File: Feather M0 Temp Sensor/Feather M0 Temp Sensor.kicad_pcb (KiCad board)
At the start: 2 copper layers, 40.6 x 25.4 mm, 3 parts, among them J1 Feather_Long_Side, J2 Feather_Short_Side, U1 Adafruit_SHT4x

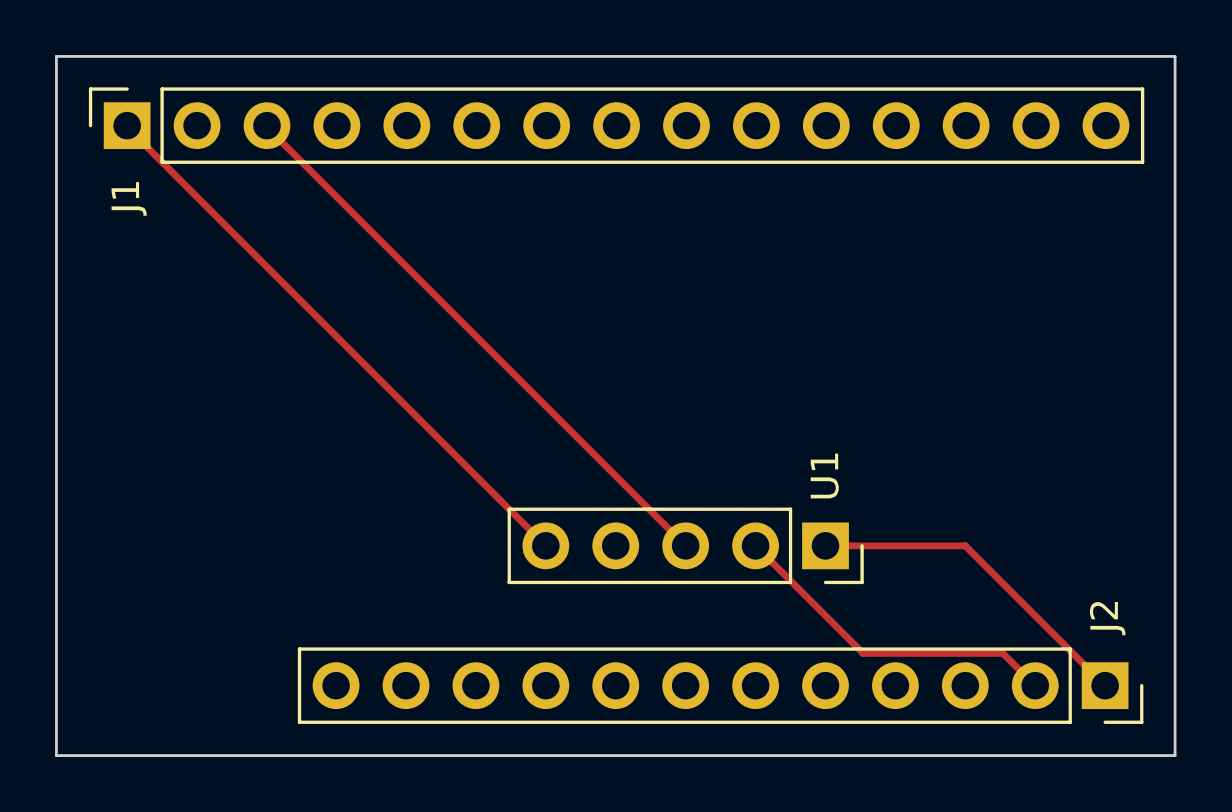
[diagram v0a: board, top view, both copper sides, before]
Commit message: Improved PCB look
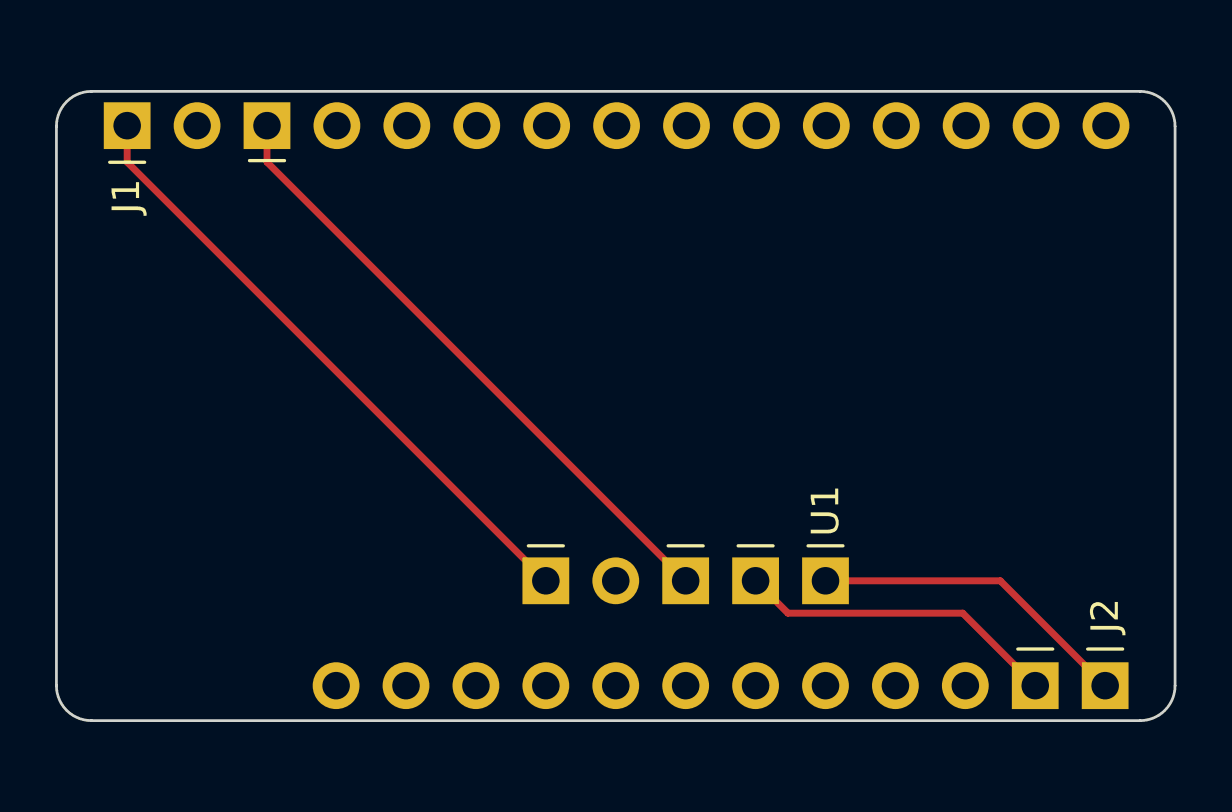
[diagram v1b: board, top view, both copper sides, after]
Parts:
- moved U1 1.27 mm to (119.4, 72.4)
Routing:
- net Net-(U1-Pad5): track 21.6 -> 22.8 mm
- net Net-(U1-Pad3): track 21.6 -> 22.8 mm
- net Net-(U1-Pad2): track 12.3 -> 11.7 mm
- net Net-(U1-Pad1): track 12.3 -> 11.7 mm
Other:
- board size 40.6 x 25.4 mm -> 40.6 x 22.9 mm
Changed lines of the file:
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@@
       (effects (font (size 1 1) (thickness 0.15)))
     )
-    (fp_line (start -1.33 1.27) (end -1.33 36.89) (layer "F.SilkS") (width 0.12))
-    (fp_line (start -1.33 36.89) (end 1.33 36.89) (layer "F.SilkS") (width 0.12))
-    (fp_line (start 0 -1.33) (end 1.33 -1.33) (layer "F.SilkS") (width 0.12))
-    (fp_line (start -1.33 1.27) (end 1.33 1.27) (layer "F.SilkS") (width 0.12))
-    (fp_line (start 1.33 1.27) (end 1.33 36.89) (layer "F.SilkS") (width 0.12))
-    (fp_line (start 1.33 -1.33) (end 1.33 0) (layer "F.SilkS") (width 0.12))
+    (fp_line (start -1.33 -0.635) (end -1.33 0.635) (layer "F.SilkS") (width 0.12))
+    (fp_line (start -1.27 4.445) (end -1.27 5.715) (layer "F.SilkS") (width 0.12))
     (fp_line (start 1.75 -1.8) (end 1.75 37.3) (layer "F.CrtYd") (width 0.05))
     (fp_line (start -1.8 -1.8) (end 1.75 -1.8) (layer "F.CrtYd") (width 0.05))
     (fp_line (start 1.75 37.3) (end -1.8 37.3) (layer "F.CrtYd") (width 0.05))
     (fp_line (start -1.8 37.3) (end -1.8 -1.8) (layer "F.CrtYd") (width 0.05))
-    (fp_line (start 1.27 -0.635) (end 1.27 36.83) (layer "F.Fab") (width 0.1))
-    (fp_line (start 0.635 -1.27) (end 1.27 -0.635) (layer "F.Fab") (width 0.1))
-    (fp_line (start -1.27 36.83) (end -1.27 -1.27) (layer "F.Fab") (width 0.1))
-    (fp_line (start 1.27 36.83) (end -1.27 36.83) (layer "F.Fab") (width 0.1))
-    (fp_line (start -1.27 -1.27) (end 0.635 -1.27) (layer "F.Fab") (width 0.1))
     (pad "1" thru_hole rect (at 0 0 90) (size 1.7 1.7) (drill 1) (layers *.Cu *.Mask)
       (net 5 "Net-(U1-Pad5)") (pinfunction "3V") (pintype "power_out"))
     (pad "2" thru_hole oval (at 0 2.54 90) (size 1.7 1.7) (drill 1) (layers *.Cu *.Mask)
       (net 6 "unconnected-(J1-Pad2)") (pinfunction "Pin_2") (pintype "passive"))
-    (pad "3" thru_hole oval (at 0 5.08 90) (size 1.7 1.7) (drill 1) (layers *.Cu *.Mask)
+    (pad "3" thru_hole rect (at 0 5.08 90) (size 1.7 1.7) (drill 1) (layers *.Cu *.Mask)
       (net 3 "Net-(U1-Pad3)") (pinfunction "GND") (pintype "power_out"))
     (pad "4" thru_hole oval (at 0 7.62 90) (size 1.7 1.7) (drill 1) (layers *.Cu *.Mask)
@@
   )
   (footprint "Connector_PinSocket_2.54mm:PinSocket_1x05_P2.54mm_Vertical" (layer "F.Cu")
-    (at 119.38 71.12 -90)
+    (at 119.38 72.39 -90)
     (descr "Through hole straight socket strip, 1x05, 2.54mm pitch, single row (from Kicad 4.0.7), script generated")
     (tags "Through hole socket strip THT 1x05 2.54mm single row")
@@
       (effects (font (size 1 1) (thickness 0.15)))
     )
-    (fp_line (start 1.33 1.27) (end 1.33 11.49) (layer "F.SilkS") (width 0.12))
-    (fp_line (start -1.33 11.49) (end 1.33 11.49) (layer "F.SilkS") (width 0.12))
-    (fp_line (start -1.33 1.27) (end 1.33 1.27) (layer "F.SilkS") (width 0.12))
-    (fp_line (start -1.33 1.27) (end -1.33 11.49) (layer "F.SilkS") (width 0.12))
-    (fp_line (start 0 -1.33) (end 1.33 -1.33) (layer "F.SilkS") (width 0.12))
-    (fp_line (start 1.33 -1.33) (end 1.33 0) (layer "F.SilkS") (width 0.12))
+    (fp_line (start -1.27 9.525) (end -1.27 10.795) (layer "F.SilkS") (width 0.12))
+    (fp_line (start -1.27 1.905) (end -1.27 3.175) (layer "F.SilkS") (width 0.12))
+    (fp_line (start -1.27 4.445) (end -1.27 5.715) (layer "F.SilkS") (width 0.12))
+    (fp_line (start -1.27 -0.635) (end -1.27 0.635) (layer "F.SilkS") (width 0.12))
     (fp_line (start 1.75 -1.8) (end 1.75 11.9) (layer "F.CrtYd") (width 0.05))
     (fp_line (start -1.8 11.9) (end -1.8 -1.8) (layer "F.CrtYd") (width 0.05))
     (fp_line (start 1.75 11.9) (end -1.8 11.9) (layer "F.CrtYd") (width 0.05))
     (fp_line (start -1.8 -1.8) (end 1.75 -1.8) (layer "F.CrtYd") (width 0.05))
-    (fp_line (start -1.27 -1.27) (end 0.635 -1.27) (layer "F.Fab") (width 0.1))
-    (fp_line (start 1.27 11.43) (end -1.27 11.43) (layer "F.Fab") (width 0.1))
-    (fp_line (start -1.27 11.43) (end -1.27 -1.27) (layer "F.Fab") (width 0.1))
-    (fp_line (start 0.635 -1.27) (end 1.27 -0.635) (layer "F.Fab") (width 0.1))
-    (fp_line (start 1.27 -0.635) (end 1.27 11.43) (layer "F.Fab") (width 0.1))
     (pad "1" thru_hole rect (at 0 0 270) (size 1.7 1.7) (drill 1) (layers *.Cu *.Mask)
       (net 1 "Net-(U1-Pad1)") (pinfunction "SDA") (pintype "bidirectional"))
-    (pad "2" thru_hole oval (at 0 2.54 270) (size 1.7 1.7) (drill 1) (layers *.Cu *.Mask)
+    (pad "2" thru_hole rect (at 0 2.54 270) (size 1.7 1.7) (drill 1) (layers *.Cu *.Mask)
       (net 2 "Net-(U1-Pad2)") (pinfunction "SCL") (pintype "input"))
-    (pad "3" thru_hole oval (at 0 5.08 270) (size 1.7 1.7) (drill 1) (layers *.Cu *.Mask)
+    (pad "3" thru_hole rect (at 0 5.08 270) (size 1.7 1.7) (drill 1) (layers *.Cu *.Mask)
       (net 3 "Net-(U1-Pad3)") (pinfunction "GND") (pintype "power_in"))
     (pad "4" thru_hole oval (at 0 7.62 270) (size 1.7 1.7) (drill 1) (layers *.Cu *.Mask)
       (net 4 "unconnected-(U1-Pad4)") (pinfunction "3V") (pintype "power_out"))
-    (pad "5" thru_hole oval (at 0 10.16 270) (size 1.7 1.7) (drill 1) (layers *.Cu *.Mask)
+    (pad "5" thru_hole rect (at 0 10.16 270) (size 1.7 1.7) (drill 1) (layers *.Cu *.Mask)
       (net 5 "Net-(U1-Pad5)") (pinfunction "VIN") (pintype "power_in"))
     (model "${KICAD6_3DMODEL_DIR}/Connector_PinSocket_2.54mm.3dshapes/PinSocket_1x05_P2.54mm_Vertical.wrl"
@@
       (effects (font (size 1 1) (thickness 0.15)))
     )
-    (fp_line (start 1.33 1.27) (end 1.33 29.27) (layer "F.SilkS") (width 0.12))
-    (fp_line (start 0 -1.33) (end 1.33 -1.33) (layer "F.SilkS") (width 0.12))
-    (fp_line (start -1.33 1.27) (end -1.33 29.27) (layer "F.SilkS") (width 0.12))
-    (fp_line (start -1.33 1.27) (end 1.33 1.27) (layer "F.SilkS") (width 0.12))
-    (fp_line (start 1.33 -1.33) (end 1.33 0) (layer "F.SilkS") (width 0.12))
-    (fp_line (start -1.33 29.27) (end 1.33 29.27) (layer "F.SilkS") (width 0.12))
+    (fp_line (start -1.33 -0.635) (end -1.33 0.635) (layer "F.SilkS") (width 0.12))
+    (fp_line (start -1.33 1.905) (end -1.33 3.175) (layer "F.SilkS") (width 0.12))
     (fp_line (start -1.8 29.7) (end -1.8 -1.8) (layer "F.CrtYd") (width 0.05))
     (fp_line (start -1.8 -1.8) (end 1.75 -1.8) (layer "F.CrtYd") (width 0.05))
     (fp_line (start 1.75 -1.8) (end 1.75 29.7) (layer "F.CrtYd") (width 0.05))
     (fp_line (start 1.75 29.7) (end -1.8 29.7) (layer "F.CrtYd") (width 0.05))
-    (fp_line (start -1.27 -1.27) (end 0.635 -1.27) (layer "F.Fab") (width 0.1))
-    (fp_line (start 1.27 29.21) (end -1.27 29.21) (layer "F.Fab") (width 0.1))
-    (fp_line (start -1.27 29.21) (end -1.27 -1.27) (layer "F.Fab") (width 0.1))
-    (fp_line (start 0.635 -1.27) (end 1.27 -0.635) (layer "F.Fab") (width 0.1))
-    (fp_line (start 1.27 -0.635) (end 1.27 29.21) (layer "F.Fab") (width 0.1))
     (pad "1" thru_hole rect (at 0 0 270) (size 1.7 1.7) (drill 1) (layers *.Cu *.Mask)
       (net 1 "Net-(U1-Pad1)") (pinfunction "SDA") (pintype "bidirectional"))
-    (pad "2" thru_hole oval (at 0 2.54 270) (size 1.7 1.7) (drill 1) (layers *.Cu *.Mask)
+    (pad "2" thru_hole rect (at 0 2.54 270) (size 1.7 1.7) (drill 1) (layers *.Cu *.Mask)
       (net 2 "Net-(U1-Pad2)") (pinfunction "SCL") (pintype "output"))
     (pad "3" thru_hole oval (at 0 5.08 270) (size 1.7 1.7) (drill 1) (layers *.Cu *.Mask)
@@
     )
   )
-  (gr_rect (start 132.08 78.74) (end 91.44 53.34) (layer "Edge.Cuts") (width 0.1) (fill none))
-  (segment (start 129.54 76.2) (end 124.46 71.12) (width 0.25) (layer "F.Cu") (net 1))
-  (segment (start 124.46 71.12) (end 119.38 71.12) (width 0.25) (layer "F.Cu") (net 1))
-  (segment (start 127 76.2) (end 125.825 75.025) (width 0.25) (layer "F.Cu") (net 2))
-  (segment (start 120.745 75.025) (end 116.84 71.12) (width 0.25) (layer "F.Cu") (net 2))
-  (segment (start 125.825 75.025) (end 120.745 75.025) (width 0.25) (layer "F.Cu") (net 2))
-  (segment (start 114.3 71.12) (end 99.09 55.91) (width 0.25) (layer "F.Cu") (net 3))
-  (segment (start 99.09 55.91) (end 99.09 55.855) (width 0.25) (layer "F.Cu") (net 3))
-  (segment (start 94.01 55.91) (end 109.22 71.12) (width 0.25) (layer "F.Cu") (net 5))
-  (segment (start 94.01 55.855) (end 94.01 55.91) (width 0.25) (layer "F.Cu") (net 5))
+  (gr_arc (start 91.44 55.88) (mid 91.811974 54.981974) (end 92.71 54.61) (layer "Edge.Cuts") (width 0.1))
+  (gr_arc (start 132.08 76.2) (mid 131.708026 77.098026) (end 130.81 77.47) (layer "Edge.Cuts") (width 0.1))
+  (gr_line (start 92.71 54.61) (end 130.81 54.61) (layer "Edge.Cuts") (width 0.1))
+  (gr_line (start 92.71 77.47) (end 130.81 77.47) (layer "Edge.Cuts") (width 0.1))
+  (gr_line (start 91.44 55.88) (end 91.44 76.2) (layer "Edge.Cuts") (width 0.1))
+  (gr_line (start 132.08 76.2) (end 132.08 55.88) (layer "Edge.Cuts") (width 0.1))
+  (gr_arc (start 92.71 77.47) (mid 91.811974 77.098026) (end 91.44 76.2) (layer "Edge.Cuts") (width 0.1))
+  (gr_arc (start 130.81 54.61) (mid 131.708026 54.981974) (end 132.08 55.88) (layer "Edge.Cuts") (width 0.1))
+  (segment (start 119.38 72.39) (end 125.73 72.39) (width 0.25) (layer "F.Cu") (net 1))
+  (segment (start 125.73 72.39) (end 129.54 76.2) (width 0.25) (layer "F.Cu") (net 1))
+  (segment (start 124.365 73.565) (end 127 76.2) (width 0.25) (layer "F.Cu") (net 2))
+  (segment (start 116.84 72.39) (end 118.015 73.565) (width 0.25) (layer "F.Cu") (net 2))
+  (segment (start 118.015 73.565) (end 124.365 73.565) (width 0.25) (layer "F.Cu") (net 2))
+  (segment (start 99.09 55.855) (end 99.09 57.18) (width 0.25) (layer "F.Cu") (net 3))
+  (segment (start 99.09 57.18) (end 114.3 72.39) (width 0.25) (layer "F.Cu") (net 3))
+  (segment (start 94.01 55.855) (end 94.01 57.18) (width 0.25) (layer "F.Cu") (net 5))
+  (segment (start 94.01 57.18) (end 109.22 72.39) (width 0.25) (layer "F.Cu") (net 5))
 )

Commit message: feat: Redesign PCB for A0 SHT power
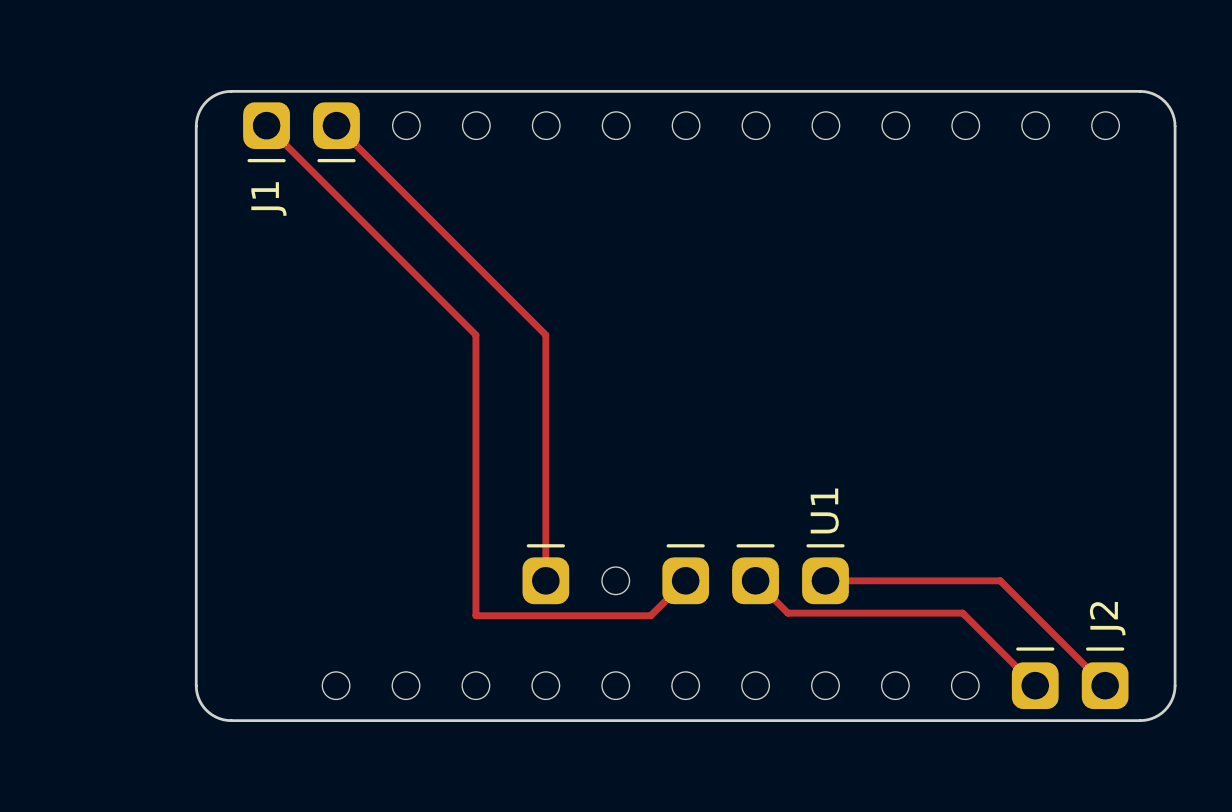
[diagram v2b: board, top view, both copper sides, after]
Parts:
- J1: footprint Connector_PinSocket_2.54mm:PinSocket_1x15_P2.54mm_Vertical -> Connector_PinSocket_2.54mm:PinSocket_1x13_P2.54mm_Vertical
- moved J1 5.06 mm to (99.1, 55.9)
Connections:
- J1 pad 1: Net-(U1-Pad5) -> Net-(U1-Pad3)
- J1 pad 10: unconnected-(J1-Pad10) -> (no net)
- J1 pad 11: unconnected-(J1-Pad11) -> (no net)
- J1 pad 12: unconnected-(J1-Pad12) -> (no net)
- J1 pad 13: unconnected-(J1-Pad13) -> (no net)
- J1 pad 2: unconnected-(J1-Pad2) -> Net-(U1-Pad5)
- J1 pad 3: Net-(U1-Pad3) -> (no net)
- J1 pad 4: unconnected-(J1-Pad4) -> (no net)
- J1 pad 5: unconnected-(J1-Pad5) -> (no net)
- J1 pad 6: unconnected-(J1-Pad6) -> (no net)
- J1 pad 7: unconnected-(J1-Pad7) -> (no net)
- J1 pad 8: unconnected-(J1-Pad8) -> (no net)
- J1 pad 9: unconnected-(J1-Pad9) -> (no net)
- J2 pad 10: unconnected-(J2-Pad10) -> (no net)
- J2 pad 11: unconnected-(J2-Pad11) -> (no net)
- J2 pad 12: unconnected-(J2-Pad12) -> (no net)
- J2 pad 3: unconnected-(J2-Pad3) -> (no net)
- J2 pad 4: unconnected-(J2-Pad4) -> (no net)
- J2 pad 5: unconnected-(J2-Pad5) -> (no net)
- J2 pad 6: unconnected-(J2-Pad6) -> (no net)
- J2 pad 7: unconnected-(J2-Pad7) -> (no net)
- J2 pad 8: unconnected-(J2-Pad8) -> (no net)
- J2 pad 9: unconnected-(J2-Pad9) -> (no net)
- U1 pad 4: unconnected-(U1-Pad4) -> (no net)
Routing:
- net Net-(U1-Pad3): track 22.8 -> 29.1 mm
- net Net-(U1-Pad5): track 22.8 -> 19.7 mm
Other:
- board size 40.6 x 22.9 mm -> 35.6 x 22.9 mm
